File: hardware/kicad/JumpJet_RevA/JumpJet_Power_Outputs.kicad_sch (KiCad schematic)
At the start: 44 parts, among them J1 24V IN / 20A MIN, J2 PTC 24V / 200W, J3 4-WIRE FAN: 24V/GND/TACH/PWM, J4 AUX1 DNP, Q1 60V NFET TBD, Q2 2N7002-CLASS PWM OD PROVISION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, Q3 60V NFET DNP, Q4 Q_GATE_EN 2N7002-CLASS PROVIS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, U1 SN74LV4T125

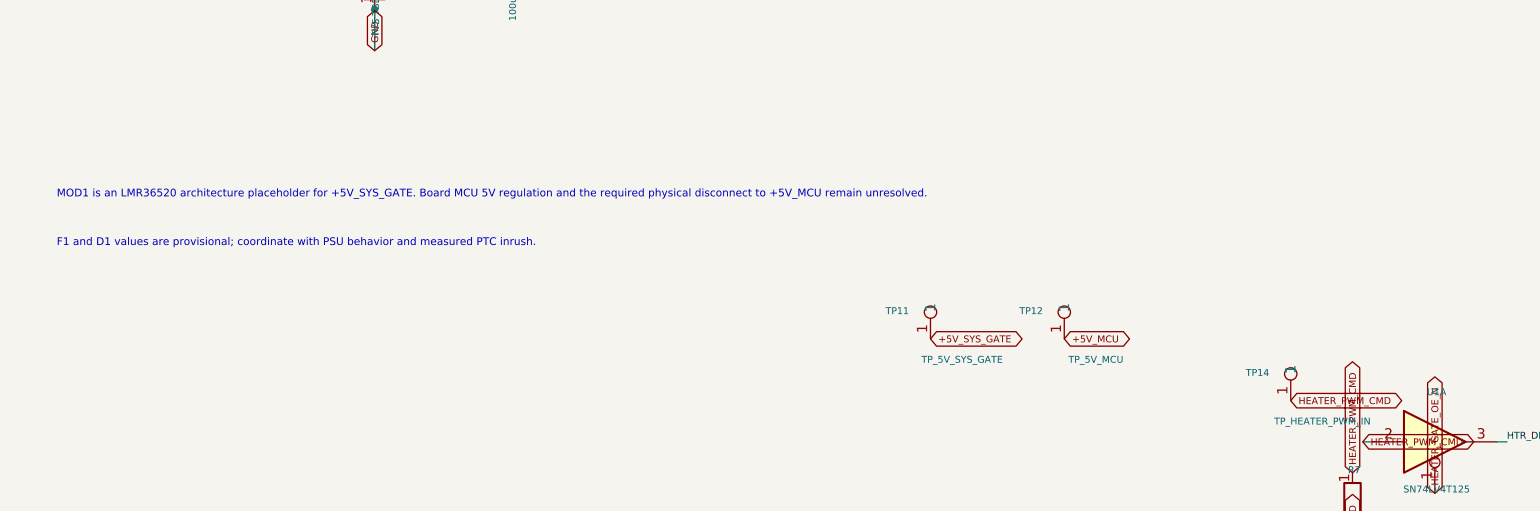
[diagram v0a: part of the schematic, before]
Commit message: hardware: implement MCU power isolation and service disconnect
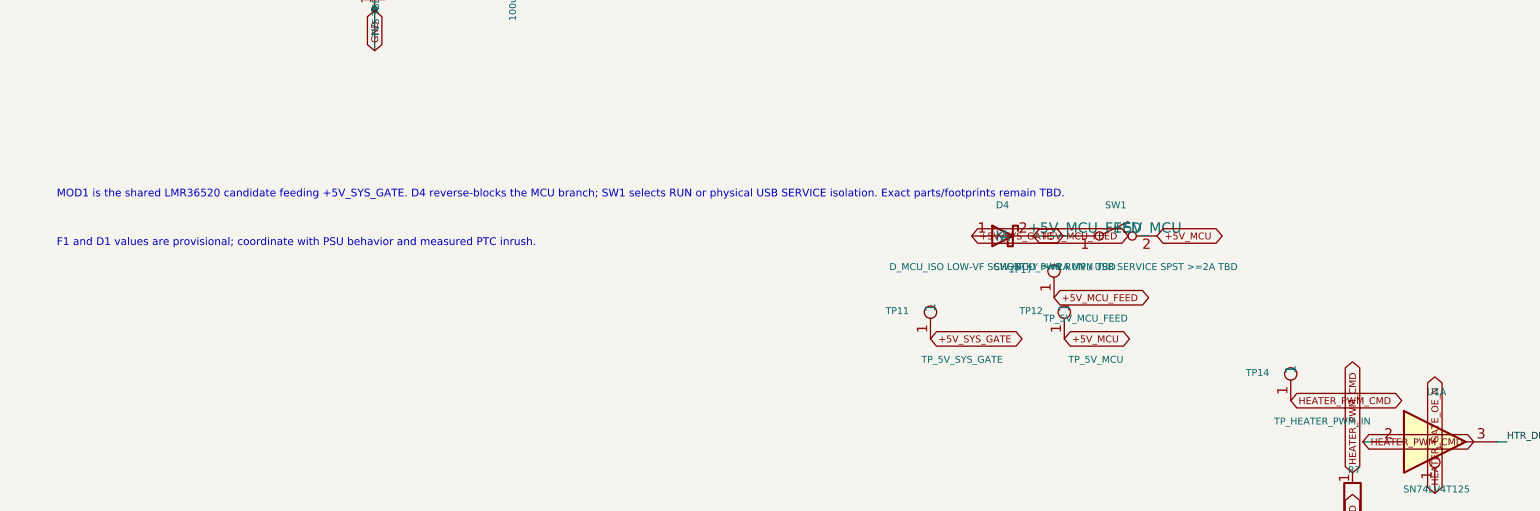
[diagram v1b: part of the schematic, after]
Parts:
- added D4: D_MCU_ISO LOW-VF SCHOTTKY >=2A MPN TBD, symbol JumpJet_Controller_RevA:JJ_MCU_ISOLATOR
- added SW1: SW_MCU_PWR RUN / USB SERVICE SPST >=2A TBD, symbol JumpJet_Controller_RevA:JJ_MCU_PWR_DISCONNECT
- added TP17: TP_5V_MCU_FEED, TestPoint:TestPoint_Pad_D1.5mm, symbol Connector:TestPoint
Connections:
- net +5V_MCU: now also SW1.2 (+5V_MCU)
- net +5V_SYS_GATE: now also D4.1 (A)
- new net +5V_MCU_FEED: D4.2 (K), SW1.1 (+5V_MCU_FEED), TP17.1
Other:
- note added: "MOD1 is the shared LMR36520 candidate feeding +5V_SYS_GATE. D4 reverse-blocks the MCU branch; SW1 selects RUN or physical USB SERVICE isolation. Exact parts/footprints remain TBD."
- note removed: "MOD1 is an LMR36520 architecture placeholder for +5V_SYS_GATE. Board MCU 5V regulation and the required physical disconnect to +5V_MCU remain unresolved."
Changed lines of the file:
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@@
+    (stroke (width 0) (type default))
+  )
+  (wire (pts (xy 143.51 96.52) (xy 148.59 96.52))
     (stroke (width 0) (type default))
   )
@@
     (effects (font (size 1.80 1.80) (thickness 0.225)) (justify left bottom))
   )
-  (text "MOD1 is an LMR36520 architecture placeholder for +5V_SYS_GATE. Board MCU 5V regulation and the required physical disconnect to +5V_MCU remain unresolved."
+  (text "MOD1 is the shared LMR36520 candidate feeding +5V_SYS_GATE. D4 reverse-blocks the MCU branch; SW1 selects RUN or physical USB SERVICE isolation. Exact parts/footprints remain TBD."
     (at 23.00 92.00 0)
     (effects (font (size 0.95 0.95) (thickness 0.120)) (justify left bottom))
@@
   )
   (global_label "+5V_MCU" (shape bidirectional) (at 147.32 109.22 0) (fields_autoplaced)
+    (effects (font (size 0.85 0.85)) (justify left bottom))
+  )
+  (global_label "+5V_SYS_GATE" (shape bidirectional) (at 135.89 96.52 0) (fields_autoplaced)
+    (effects (font (size 0.85 0.85)) (justify left bottom))
+  )
+  (global_label "+5V_MCU_FEED" (shape bidirectional) (at 146.05 104.14 0) (fields_autoplaced)
+    (effects (font (size 0.85 0.85)) (justify left bottom))
+  )
+  (global_label "+5V_MCU_FEED" (shape bidirectional) (at 143.51 96.52 0) (fields_autoplaced)
+    (effects (font (size 0.85 0.85)) (justify left bottom))
+  )
+  (global_label "+5V_MCU" (shape bidirectional) (at 158.75 96.52 0) (fields_autoplaced)
     (effects (font (size 0.85 0.85)) (justify left bottom))
   )
@@
     )
   )
+  (symbol (lib_id "JumpJet_Controller_RevA:JJ_MCU_ISOLATOR") (at 139.7 96.52 0) (unit 1)
+    (in_bom yes) (on_board yes) (dnp no)
+    (property "Reference" "D4" (at 139.7 92.71 0)
+      (effects (font (size 0.85 0.85)))
+    )
+    (property "Value" "D_MCU_ISO LOW-VF SCHOTTKY >=2A MPN TBD" (at 139.7 100.33 0)
+      (effects (font (size 0.85 0.85)))
+    )
+    (property "Footprint" "" (at 139.7 96.52 0)
+      (effects (font (size 0.85 0.85)) hide)
+    )
+    (property "Datasheet" "" (at 139.7 96.52 0)
+      (effects (font (size 0.85 0.85)) hide)
+    )
+    (property "Description" "Strong-candidate low-Vf Schottky reverse blocker; exact MPN and footprint TBD after current, leakage, thermal, and availability review." (at 139.7 96.52 0)
+      (effects (font (size 0.85 0.85)) hide)
+    )
+    (pin "1")
+    (pin "2")
+    (instances
+      (project "JumpJet_Controller_RevA4"
+        (path "/7daa19f2-c821-405d-9b33-9c66dc62ede9"
+          (reference "D4") (unit 1)
+        )
+      )
+    )
+  )
+  (symbol (lib_id "JumpJet_Controller_RevA:JJ_MCU_PWR_DISCONNECT") (at 153.67 96.52 0) (unit 1)
+    (in_bom yes) (on_board yes) (dnp no)
+    (property "Reference" "SW1" (at 153.67 92.71 0)
+      (effects (font (size 0.85 0.85)))
+    )
+    (property "Value" "SW_MCU_PWR RUN / USB SERVICE SPST >=2A TBD" (at 153.67 100.33 0)
+      (effects (font (size 0.85 0.85)))
+    )
+    (property "Footprint" "" (at 153.67 96.52 0)
+      (effects (font (size 0.85 0.85)) hide)
+    )
+    (property "Datasheet" "" (at 153.67 96.52 0)
+      (effects (font (size 0.85 0.85)) hide)
+    )
+    (property "Description" "Strong-candidate physical SPST slide-switch class for RUN / USB SERVICE isolation; exact MPN and footprint TBD after current, contact-resistance, temperature, retention, and service-edge review." (at 153.67 96.52 0)
+      (effects (font (size 0.85 0.85)) hide)
+    )
+    (pin "1")
+    (pin "2")
+    (instances
+      (project "JumpJet_Controller_RevA4"
+        (path "/7daa19f2-c821-405d-9b33-9c66dc62ede9"
+          (reference "SW1") (unit 1)
+        )
+      )
+    )
+  )
+  (symbol (lib_id "Connector:TestPoint") (at 146.05 104.14 0) (unit 1)
+    (in_bom yes) (on_board yes) (dnp no)
+    (property "Reference" "TP17" (at 141.95 100.69 0) (effects (font (size 0.85 0.85))))
+    (property "Value" "TP_5V_MCU_FEED" (at 149.95 106.69 0) (effects (font (size 0.85 0.85))))
+    (property "Footprint" "TestPoint:TestPoint_Pad_D1.5mm" (at 145.95 103.69 0) (effects (font (size 0.85 0.85)) hide))
+    (property "Datasheet" "" (at 145.95 103.69 0) (effects (font (size 0.85 0.85)) hide))
+    (property "Description" "Board-derived MCU feed test point between reverse blocker and RUN / USB SERVICE switch." (at 145.95 103.69 0) (effects (font (size 0.85 0.85)) hide))
+    (pin "1")
+    (instances (project "JumpJet_Controller_RevA4" (path "/7daa19f2-c821-405d-9b33-9c66dc62ede9" (reference "TP17") (unit 1))))
+  )
   (symbol (lib_id "Connector:TestPoint") (at 130.81 109.22 0) (unit 1)
